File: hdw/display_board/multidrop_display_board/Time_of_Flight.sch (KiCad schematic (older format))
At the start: 7 parts, among them U1501 DS1683

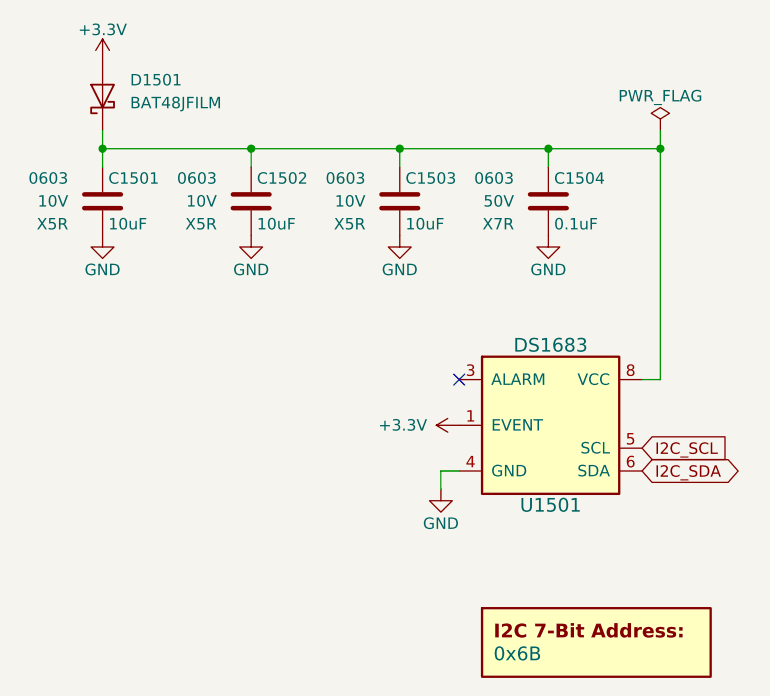
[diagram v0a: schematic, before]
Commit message: renamed project, added segments, transceivers
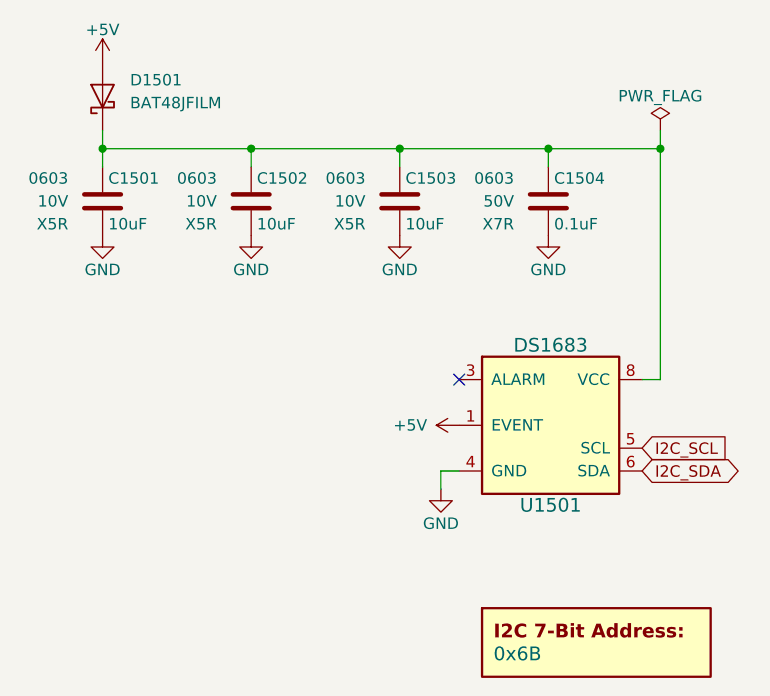
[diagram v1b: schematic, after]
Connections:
- net +3V3 renamed +5V
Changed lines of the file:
@@
 EESchema Schematic File Version 4
+LIBS:multidrop_display_board-cache
 EELAYER 30 0
 EELAYER END
@@
 I2C_SDA
 $Comp
-L power:+3.3V #PWR01506
-U 1 1 5E36CA22
-P 4440 4100
-F 0 "#PWR01506" H 4440 3950 50  0001 C CNN
-F 1 "+3.3V" V 4440 4240 50  0000 L CNN
-F 2 "" H 4440 4100 50  0001 C CNN
-F 3 "" H 4440 4100 50  0001 C CNN
-	1    4440 4100
-	0    -1   -1   0
-$EndComp
-$Comp
-L power:+3.3V #PWR01501
-U 1 1 5E36D120
-P 2880 2510
-F 0 "#PWR01501" H 2880 2360 50  0001 C CNN
-F 1 "+3.3V" H 2880 2650 50  0000 C CNN
-F 2 "" H 2880 2510 50  0001 C CNN
-F 3 "" H 2880 2510 50  0001 C CNN
-	1    2880 2510
-	1    0    0    -1
-$EndComp
-$Comp
 L power:PWR_FLAG #FLG01501
 U 1 1 5E4BADF7
@@
 	0    -1   -1   0
 $EndComp
+$Comp
+L power:+5V #PWR?
+U 1 1 5F7B4178
+P 2880 2510
+F 0 "#PWR?" H 2880 2360 50  0001 C CNN
+F 1 "+5V" H 2880 2650 50  0000 C CNN
+F 2 "" H 2880 2510 50  0001 C CNN
+F 3 "" H 2880 2510 50  0001 C CNN
+	1    2880 2510
+	1    0    0    -1
+$EndComp
+$Comp
+L power:+5V #PWR?
+U 1 1 5F7B45EE
+P 4440 4100
+F 0 "#PWR?" H 4440 3950 50  0001 C CNN
+F 1 "+5V" V 4440 4240 50  0000 L CNN
+F 2 "" H 4440 4100 50  0001 C CNN
+F 3 "" H 4440 4100 50  0001 C CNN
+	1    4440 4100
+	0    -1   -1   0
+$EndComp

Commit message: more sch work
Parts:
- removed C1501, C1502: 10uF, Capacitors_SMD:C_0603, symbol Custom_Library:C_Custom
- added C? (x2): 10uF, Capacitors_SMD:C_0603, symbol Custom_Library:C_Custom
- C1503, C1504, D1501, U1501: Configuration (none) -> TOF
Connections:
- net GND: now also C?.2, C?.2
- net at C1503.1, C1504.1, D1501.1 (K)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: now also C?.1, C?.1
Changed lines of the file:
@@
 F 3 "https://datasheets.maximintegrated.com/en/ds/DS1683.pdf" H 4740 4400 60  0001 C CNN
 F 4 "DS1683S+-ND" H 4940 3850 60  0001 C CNN "Digi-Key PN"
+F 5 "TOF" H 4840 3650 50  0000 C CNN "Configuration"
 	1    4840 4100
 	1    0    0    -1
@@
 F 6 "X7R" H 4680 3020 50  0000 R CNN "Dielectric"
 F 7 "399-7845-1-ND" H 4830 3120 50  0001 C CNN "Digi-Key PN"
+F 8 "TOF" H 4680 2930 50  0000 R CNN "Configuration"
 	1    4830 3120
 	1    0    0    -1
@@
 F 6 "10V" H 4030 3120 50  0000 R CNN "Voltage"
 F 7 "X5R" H 4030 3020 50  0000 R CNN "Dielectric"
+F 8 "TOF" H 4030 2930 50  0000 R CNN "Configuration"
 	1    4180 3120
-	1    0    0    -1
-$EndComp
-$Comp
-L Custom_Library:C_Custom C?
-U 1 1 5E2AFBB1
-P 3530 3120
-AR Path="/5C1D5CD8/5E2AFBB1" Ref="C?"  Part="1"
-AR Path="/5C1D5CCA/5E2AFBB1" Ref="C?"  Part="1"
-AR Path="/5C26E09A/5E2AFBB1" Ref="C?"  Part="1"
-AR Path="/5D739492/5E2AFBB1" Ref="C?"  Part="1"
-AR Path="/5E28CFDF/5E2AFBB1" Ref="C?"  Part="1"
-AR Path="/5E36CE18/5E2AFBB1" Ref="C?"  Part="1"
-AR Path="/5E3C80C8/5E2AFBB1" Ref="C?"  Part="1"
-AR Path="/5E3C97B4/5E2AFBB1" Ref="C?"  Part="1"
-AR Path="/5E2A7EE3/5E2AFBB1" Ref="C?"  Part="1"
-AR Path="/5E07B870/5E2AFBB1" Ref="C?"  Part="1"
-AR Path="/5E93A1E8/5E2AFBB1" Ref="C1502"  Part="1"
-AR Path="/5F74004E/5E2AFBB1" Ref="C1502"  Part="1"
-F 0 "C1502" H 3555 3220 50  0000 L CNN
-F 1 "10uF" H 3555 3020 50  0000 L CNN
-F 2 "Capacitors_SMD:C_0603" H 3568 2970 50  0001 C CNN
-F 3 "" H 3555 3220 50  0001 C CNN
-F 4 "490-10474-1-ND" H 3955 3620 60  0001 C CNN "Digi-Key PN"
-F 5 "0603" H 3380 3220 50  0000 R CNN "display_footprint"
-F 6 "10V" H 3380 3120 50  0000 R CNN "Voltage"
-F 7 "X5R" H 3380 3020 50  0000 R CNN "Dielectric"
-	1    3530 3120
-	1    0    0    -1
-$EndComp
-$Comp
-L Custom_Library:C_Custom C?
-U 1 1 5E2B068F
-P 2880 3120
-AR Path="/5C1D5CD8/5E2B068F" Ref="C?"  Part="1"
-AR Path="/5C1D5CCA/5E2B068F" Ref="C?"  Part="1"
-AR Path="/5C26E09A/5E2B068F" Ref="C?"  Part="1"
-AR Path="/5D739492/5E2B068F" Ref="C?"  Part="1"
-AR Path="/5E28CFDF/5E2B068F" Ref="C?"  Part="1"
-AR Path="/5E36CE18/5E2B068F" Ref="C?"  Part="1"
-AR Path="/5E3C80C8/5E2B068F" Ref="C?"  Part="1"
-AR Path="/5E3C97B4/5E2B068F" Ref="C?"  Part="1"
-AR Path="/5E2A7EE3/5E2B068F" Ref="C?"  Part="1"
-AR Path="/5E07B870/5E2B068F" Ref="C?"  Part="1"
-AR Path="/5E93A1E8/5E2B068F" Ref="C1501"  Part="1"
-AR Path="/5F74004E/5E2B068F" Ref="C1501"  Part="1"
-F 0 "C1501" H 2905 3220 50  0000 L CNN
-F 1 "10uF" H 2905 3020 50  0000 L CNN
-F 2 "Capacitors_SMD:C_0603" H 2918 2970 50  0001 C CNN
-F 3 "" H 2905 3220 50  0001 C CNN
-F 4 "490-10474-1-ND" H 3305 3620 60  0001 C CNN "Digi-Key PN"
-F 5 "0603" H 2730 3220 50  0000 R CNN "display_footprint"
-F 6 "10V" H 2730 3120 50  0000 R CNN "Voltage"
-F 7 "X5R" H 2730 3020 50  0000 R CNN "Dielectric"
-	1    2880 3120
 	1    0    0    -1
 $EndComp
@@
 F 3 "www.st.com/resource/en/datasheet/bat48.pdf" H 2880 2660 50  0001 C CNN
 F 4 "497-5711-1-ND" H 2880 2660 50  0001 C CNN "Digi-Key PN"
+F 5 "TOF" V 2750 2540 50  0000 R CNN "Configuration"
 	1    2880 2660
 	0    -1   -1   0
@@
 	0    -1   -1   0
 $EndComp
+$Comp
+L Custom_Library:C_Custom C?
+U 1 1 5F76928B
+P 3530 3120
+AR Path="/5C1D5CD8/5F76928B" Ref="C?"  Part="1"
+AR Path="/5C1D5CCA/5F76928B" Ref="C?"  Part="1"
+AR Path="/5C26E09A/5F76928B" Ref="C?"  Part="1"
+AR Path="/5D739492/5F76928B" Ref="C?"  Part="1"
+AR Path="/5E28CFDF/5F76928B" Ref="C?"  Part="1"
+AR Path="/5E36CE18/5F76928B" Ref="C?"  Part="1"
+AR Path="/5E3C80C8/5F76928B" Ref="C?"  Part="1"
+AR Path="/5E3C97B4/5F76928B" Ref="C?"  Part="1"
+AR Path="/5E2A7EE3/5F76928B" Ref="C?"  Part="1"
+AR Path="/5E07B870/5F76928B" Ref="C?"  Part="1"
+AR Path="/5E93A1E8/5F76928B" Ref="C?"  Part="1"
+AR Path="/5F74004E/5F76928B" Ref="C?"  Part="1"
+F 0 "C?" H 3555 3220 50  0000 L CNN
+F 1 "10uF" H 3555 3020 50  0000 L CNN
+F 2 "Capacitors_SMD:C_0603" H 3568 2970 50  0001 C CNN
+F 3 "" H 3555 3220 50  0001 C CNN
+F 4 "490-10474-1-ND" H 3955 3620 60  0001 C CNN "Digi-Key PN"
+F 5 "0603" H 3380 3220 50  0000 R CNN "display_footprint"
+F 6 "10V" H 3380 3120 50  0000 R CNN "Voltage"
+F 7 "X5R" H 3380 3020 50  0000 R CNN "Dielectric"
+F 8 "TOF" H 3380 2930 50  0000 R CNN "Configuration"
+	1    3530 3120
+	1    0    0    -1
+$EndComp
+$Comp
+L Custom_Library:C_Custom C?
+U 1 1 5F769832
+P 2880 3120
+AR Path="/5C1D5CD8/5F769832" Ref="C?"  Part="1"
+AR Path="/5C1D5CCA/5F769832" Ref="C?"  Part="1"
+AR Path="/5C26E09A/5F769832" Ref="C?"  Part="1"
+AR Path="/5D739492/5F769832" Ref="C?"  Part="1"
+AR Path="/5E28CFDF/5F769832" Ref="C?"  Part="1"
+AR Path="/5E36CE18/5F769832" Ref="C?"  Part="1"
+AR Path="/5E3C80C8/5F769832" Ref="C?"  Part="1"
+AR Path="/5E3C97B4/5F769832" Ref="C?"  Part="1"
+AR Path="/5E2A7EE3/5F769832" Ref="C?"  Part="1"
+AR Path="/5E07B870/5F769832" Ref="C?"  Part="1"
+AR Path="/5E93A1E8/5F769832" Ref="C?"  Part="1"
+AR Path="/5F74004E/5F769832" Ref="C?"  Part="1"
+F 0 "C?" H 2905 3220 50  0000 L CNN
+F 1 "10uF" H 2905 3020 50  0000 L CNN
+F 2 "Capacitors_SMD:C_0603" H 2918 2970 50  0001 C CNN
+F 3 "" H 2905 3220 50  0001 C CNN
+F 4 "490-10474-1-ND" H 3305 3620 60  0001 C CNN "Digi-Key PN"
+F 5 "0603" H 2730 3220 50  0000 R CNN "display_footprint"
+F 6 "10V" H 2730 3120 50  0000 R CNN "Voltage"
+F 7 "X5R" H 2730 3020 50  0000 R CNN "Dielectric"
+F 8 "TOF" H 2730 2930 50  0000 R CNN "Configuration"
+	1    2880 3120
+	1    0    0    -1
+$EndComp
 $EndSCHEMATC
